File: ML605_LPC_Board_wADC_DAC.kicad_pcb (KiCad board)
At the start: 4 copper layers, 100 x 100 mm, 118 parts, among them IC1 ADC10D040CIVS_NOPB, IC2 AD8137YRZ-REEL, IC3 AD8137YRZ-REEL, IC4 DAC5652IPFB, J1 ASP-134604-01, J10 Conn_02x06_Odd_Even, J11 Conn_02x06_Odd_Even, J12 Conn_02x06_Odd_Even, J13 Conn_01x03_Pin, J14 Conn_01x03_Pin, J2 Conn_01x03_Pin, J3 Conn_01x03_Pin, J4 SMA Connector, J5 SMA Connector, J6 Conn_01x03_Pin, J7 Conn_01x03_Pin, J8 SMA Connector, J9 SMA Connector, U1 LMV7219M7, U2 LMV7219M7, U3 NCV317, U4 LMH6702MA, U5 LMH6702MA

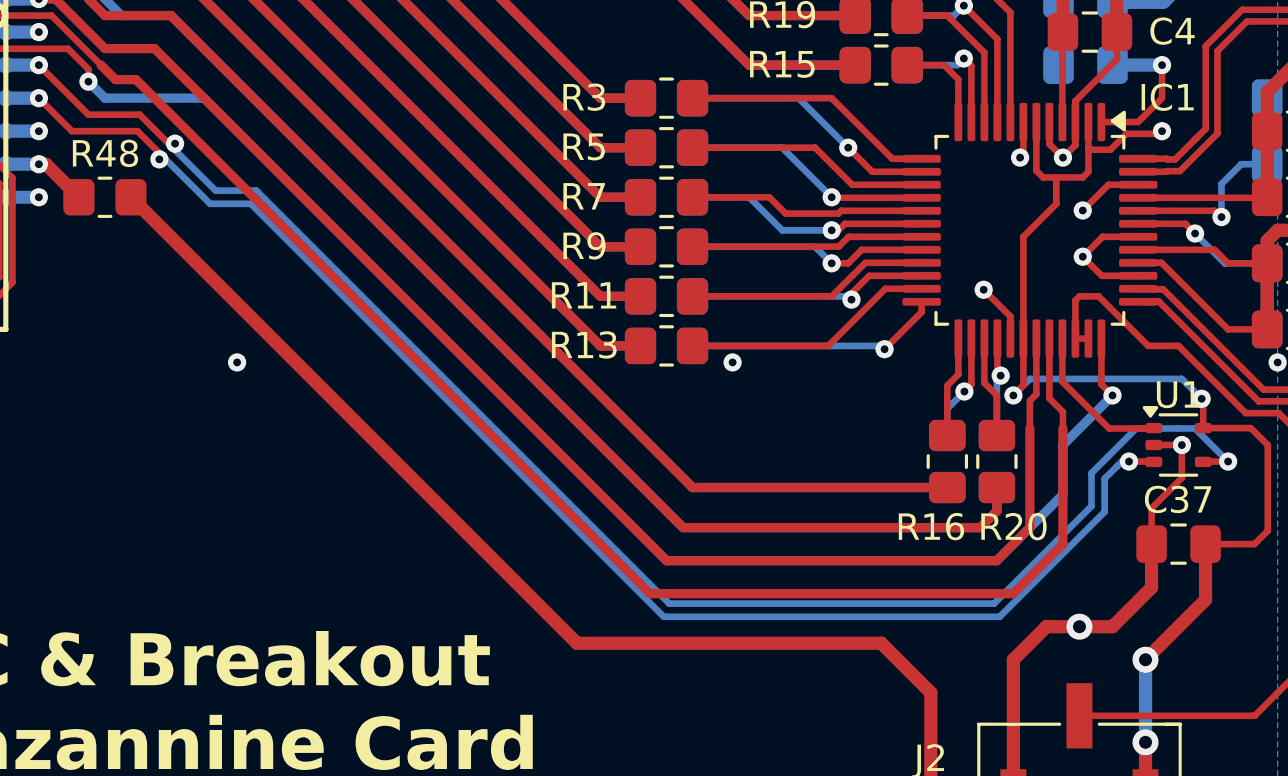
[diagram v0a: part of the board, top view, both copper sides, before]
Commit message: Did some length matching for the ADC clock differential pair
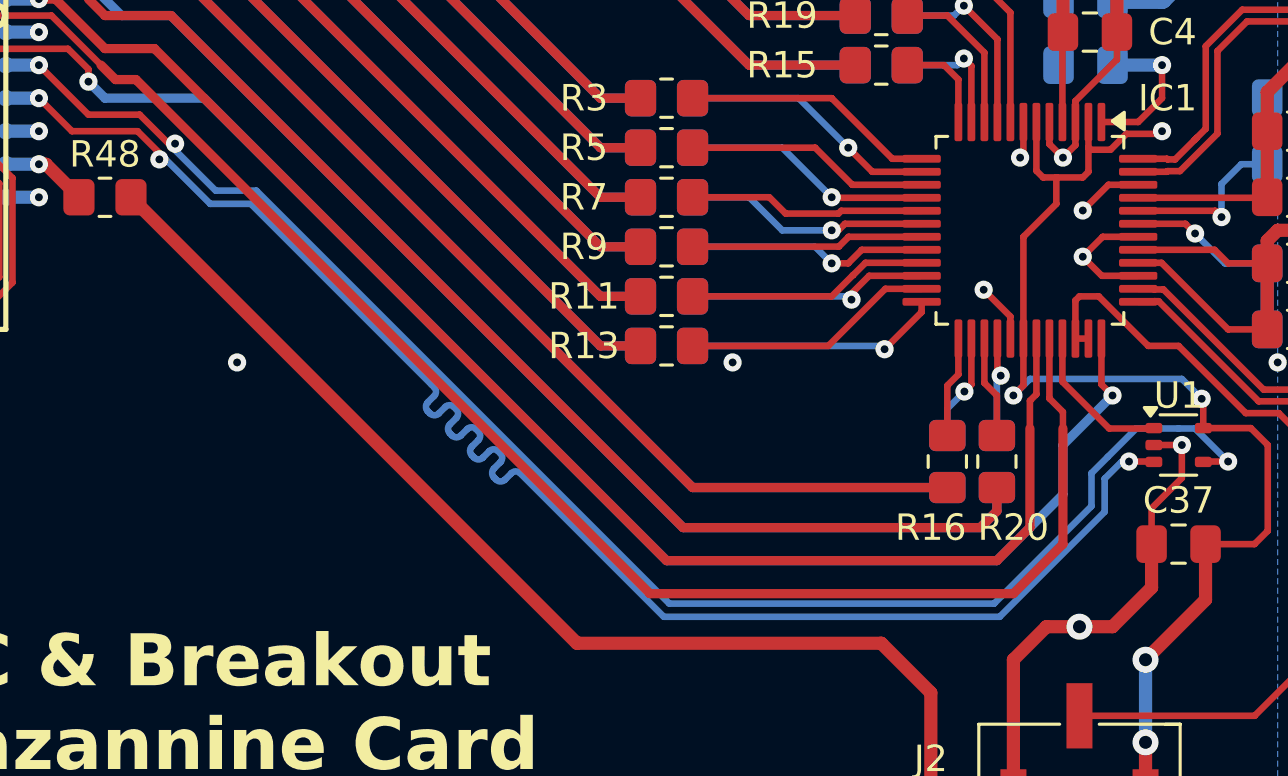
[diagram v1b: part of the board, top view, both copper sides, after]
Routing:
- net /CLK0_M2C_P: track 55.8 -> 60.6 mm

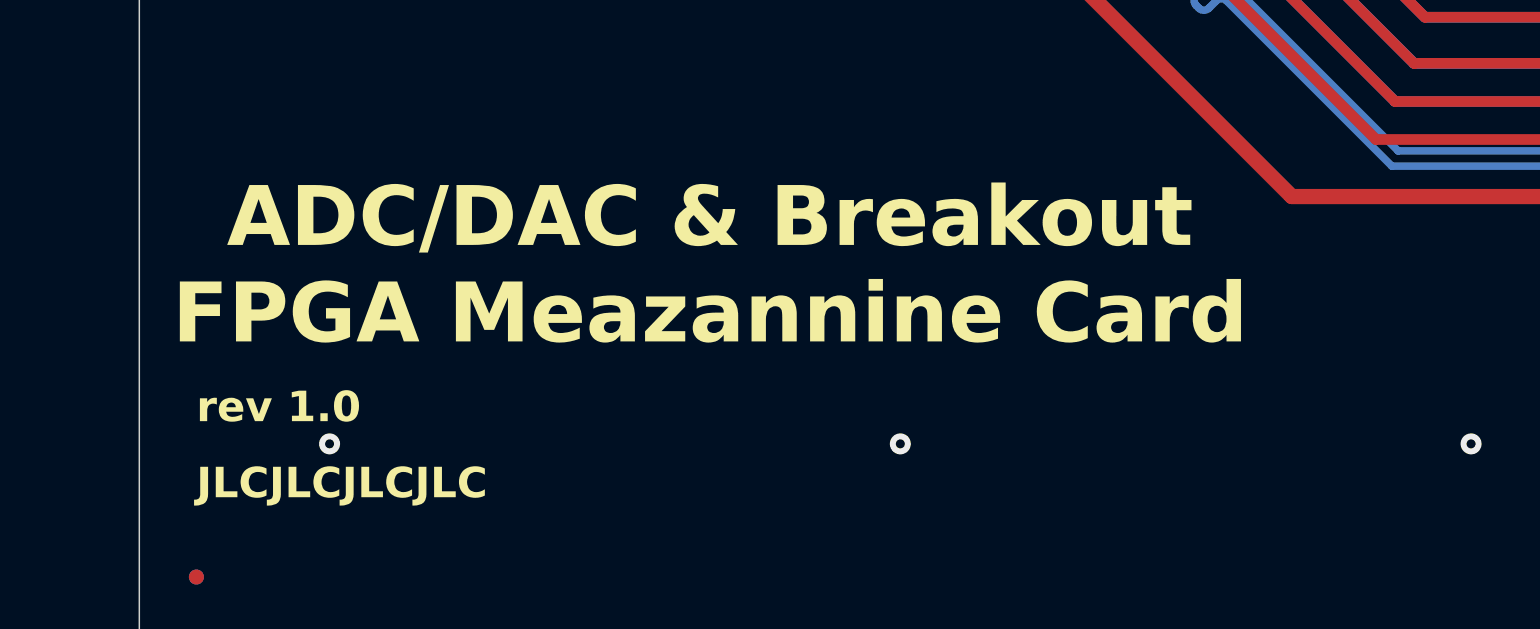
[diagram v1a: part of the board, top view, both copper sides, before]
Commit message: Review photos and Mezzaninne spelling mistake fixed
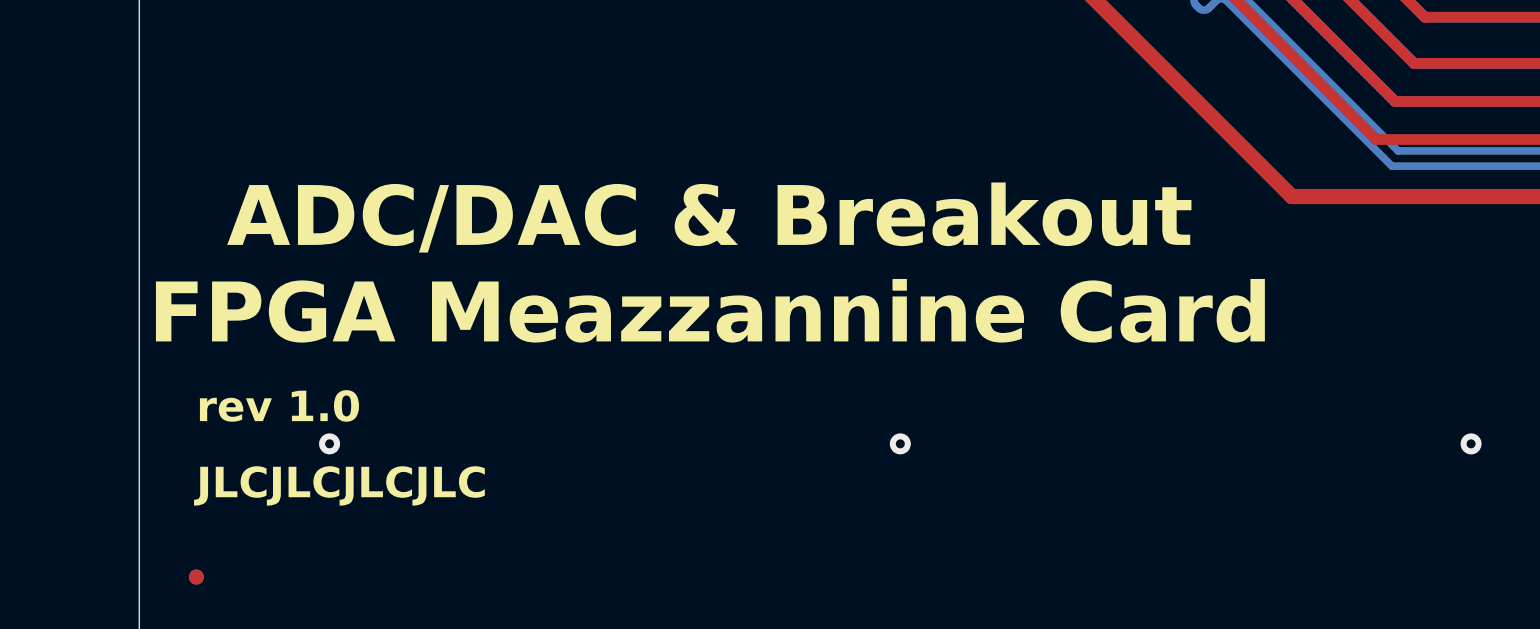
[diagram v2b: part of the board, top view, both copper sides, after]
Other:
- board text added: "ADC/DAC & Breakout FPGA Meazzannine Card"
- board text removed: "ADC/DAC & Breakout FPGA Meazannine Card"
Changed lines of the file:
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@@
 		)
 	)
-	(gr_text "ADC/DAC & Breakout\nFPGA Meazannine Card"
+	(gr_text "ADC/DAC & Breakout\nFPGA Meazzannine Card"
 		(at 94.05 140.475 0)
 		(layer "F.SilkS" knockout)

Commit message: Error in schematic, DAC output opamp is LMH6720, not LMH6702
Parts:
- U4, U5: value LMH6702MA -> LMH6720MA
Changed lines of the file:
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@@
 			)
 		)
-		(property "Value" "LMH6702MA"
+		(property "Value" "LMH6720MA"
 			(at 0 3.4 0)
 			(layer "F.Fab")
@@
 			)
 		)
-		(property "Value" "LMH6702MA"
+		(property "Value" "LMH6720MA"
 			(at 0 3.4 0)
 			(layer "F.Fab")

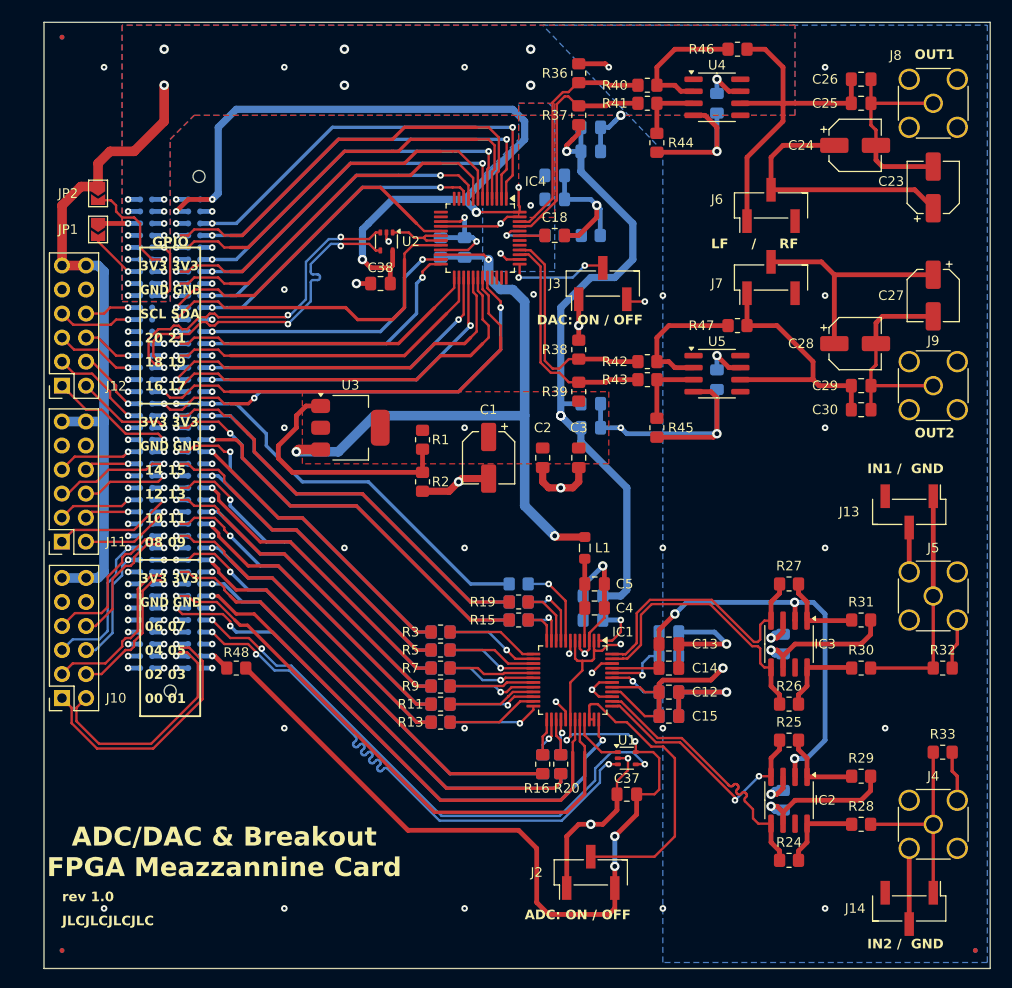
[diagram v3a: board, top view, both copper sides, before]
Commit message: Rev 1.1
Multiple changes are made, as per suggestions made by the redditors of r/PrintedCircuitBoards. Firstly, two 50 ohm resistors were added in series with the DAC output in order to comply with the minimum peak output current of the op-amps of 50mA. Secondly, two M3 mounting holes were added in order to have the possibility to add standoffs. Thirdly, a clearance issue regarding jumpers near the LPC connector on the ML602 board was fixed by changing the board geometry to include a cutout for these.

Some other things to look into are the use of some ferrite beads for supplies of the analog ICs.
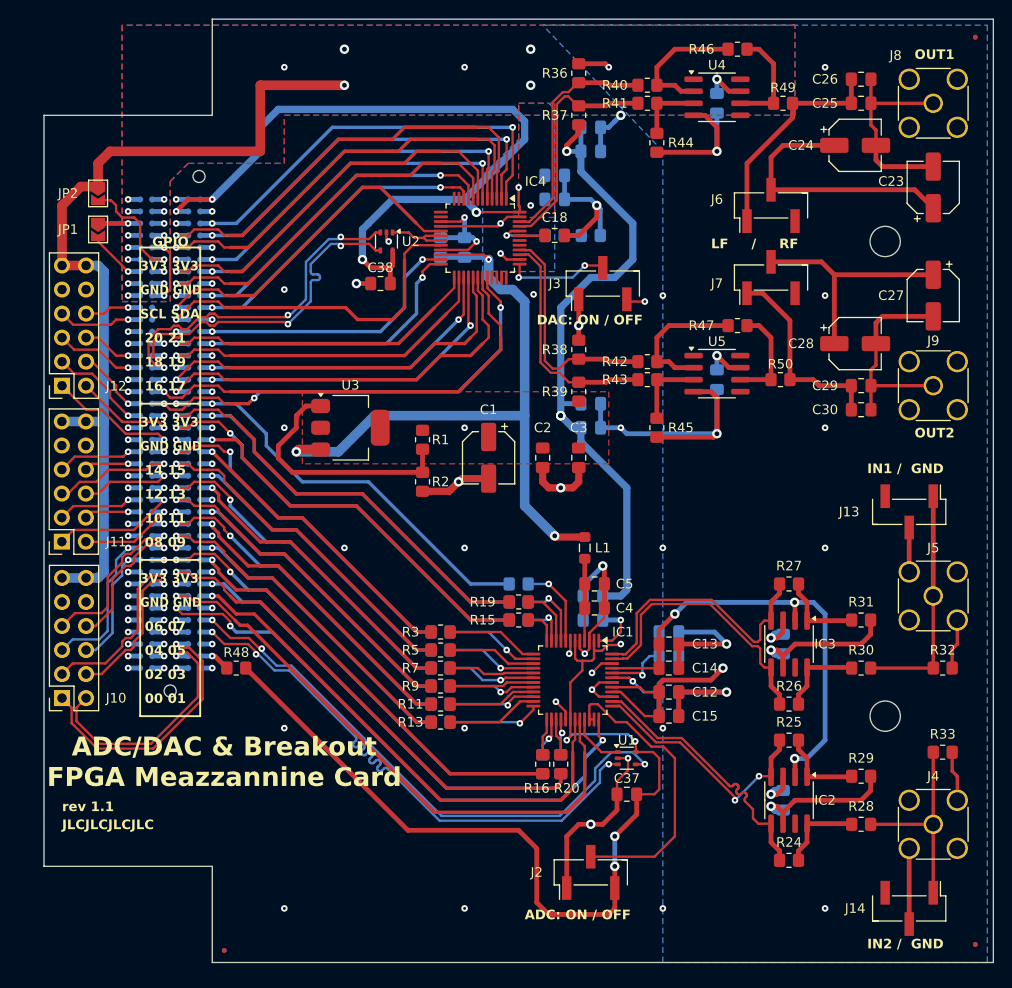
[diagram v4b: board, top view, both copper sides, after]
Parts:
- added H1: MountingHole, MountingHole:MountingHole_3.2mm_M3, F.Cu at (163.9, 73.2)
- added H2: MountingHole, MountingHole:MountingHole_3.2mm_M3, F.Cu at (163.9, 123.3)
- added R49: 50, Resistor_SMD:R_0805_2012Metric_Pad1.20x1.40mm_HandSolder, F.Cu at (153.1, 58.6)
- added R50: 50, Resistor_SMD:R_0805_2012Metric_Pad1.20x1.40mm_HandSolder, F.Cu at (152.8, 87.8)
- moved FID1 96.5 mm to (173.4, 51.6)
- moved FID4 96.5 mm to (173.4, 51.6)
- moved FID3 17.1 mm to (94.0, 148.1)
- moved FID5 17.1 mm to (94.0, 148.1)
- moved FID2 0.63 mm to (173.4, 147.5)
- moved FID6 0.63 mm to (173.4, 147.5)
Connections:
- net /LA01_N renamed /LA01_N_CC
- net /LA01_P renamed /LA01_P_CC
- R46 pad 2: Net-(J6-Pin_1) -> Net-(R46-Pad2)
- R47 pad 2: Net-(J7-Pin_1) -> Net-(R47-Pad2)
- U4 pad 6: Net-(J6-Pin_1) -> Net-(R46-Pad2)
- U5 pad 6: Net-(J7-Pin_1) -> Net-(R47-Pad2)
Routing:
- net 3V3: track 206.0 -> 226.9 mm, vias 21 -> 19
- net Net-(J6-Pin_1): track 36.7 -> 23.2 mm
- net Net-(R46-Pad2): track 0.00 -> 11.1 mm
- net Net-(R47-Pad2): track 0.00 -> 10.8 mm
- net Net-(J7-Pin_1): track 28.4 -> 21.3 mm
- net VADJ: track 255.6 -> 253.0 mm
- net GNDA: vias 111 -> 108
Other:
- board size 100 x 100 mm -> 100.3 x 99.7 mm
- board text added: "rev 1.1"
- board text removed: "rev 1.0"

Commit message: Reduced horizontal board dimension a bit
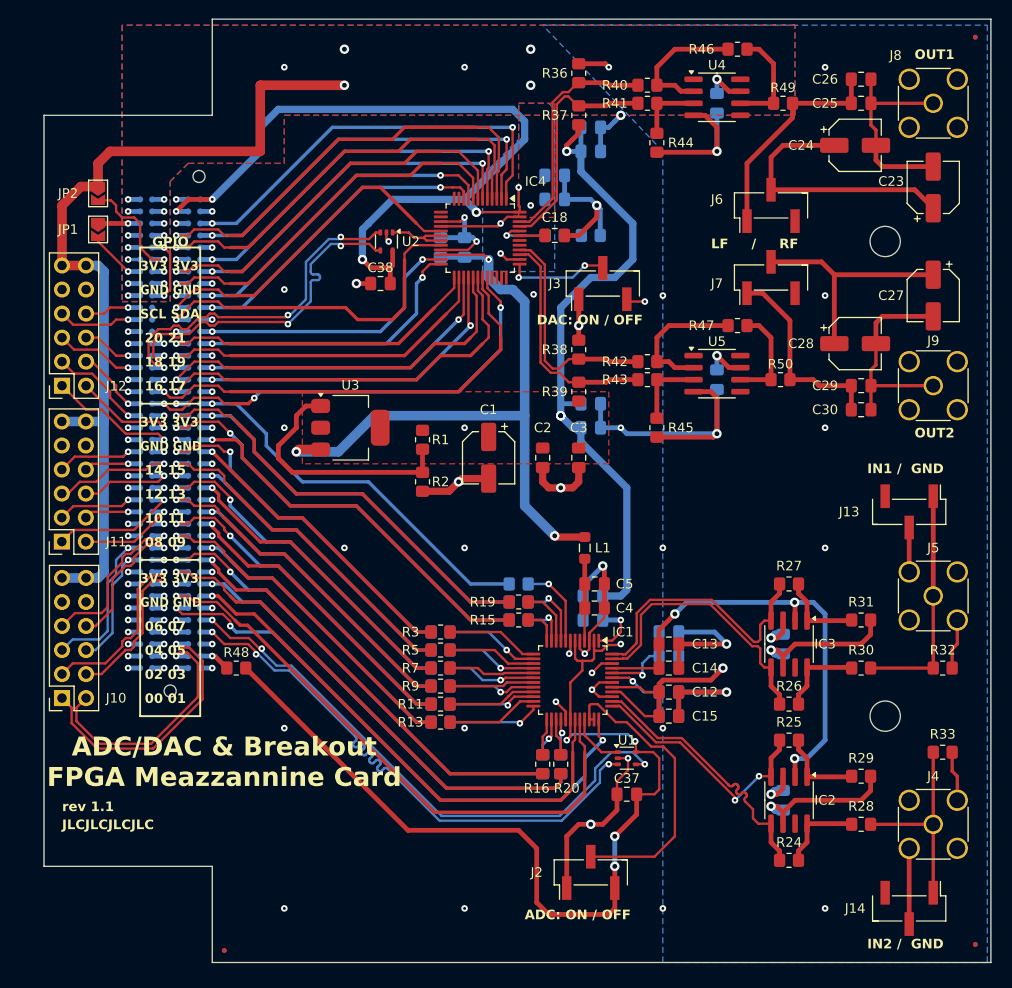
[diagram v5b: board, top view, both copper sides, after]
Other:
- board size 100.3 x 99.7 mm -> 100.1 x 99.7 mm
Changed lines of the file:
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@@
 	(gr_poly
 		(pts
-			(xy 75 139.205) (xy 75 59.83) (xy 92.78 59.83) (xy 92.78 49.67) (xy 175.33 49.67) (xy 175.33 149.365)
+			(xy 75 139.205) (xy 75 59.83) (xy 92.78 59.83) (xy 92.78 49.67) (xy 175.076 49.67) (xy 175.076 149.365)
 			(xy 92.78 149.365) (xy 92.78 139.205)
 		)
@@
 		(polygon
 			(pts
-				(xy 75 49.67) (xy 175.33 49.67) (xy 175.33 149.365) (xy 75 149.365)
+				(xy 75 49.67) (xy 175.076 49.67) (xy 175.076 149.365) (xy 75 149.365)
 			)
 		)
